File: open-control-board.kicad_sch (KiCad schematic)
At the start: 123 parts, among them CN1 Service boiler fill sensor, CN10 LCC Port, CN2 Water tank level switch, CN3 NTC Service Boiler, CN4 NTC Brew Boiler, CN5 Service boiler relay, CN6 Conn_02x04_Counter_Clockwise, CN7 Brew Switch, CN8 12V Separate Supply, CN9 Brew boiler relay, J1 USB_B_Micro, J10 Conn_01x04_Pin, J11 Conn_01x04_Pin, J12 Conn_02x06_Odd_Even, J13 Conn_02x05_Odd_Even, J14 Conn_02x04_Odd_Even, J15 Conn_02x05_Odd_Even, J16 USB_B_Micro, J18 Conn_01x03_Pin, J5 BM04B-SRSS-TB(LF)(SN), Q1 AO3401A, Q11 DMN63D8LDW, Q2 AO3401A, Q3 Q_PMOS-E_DUAL_Generic_SEP_S1G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, Q4 DMN63D8LDW, Q5 Q_PMOS-E_DUAL_Generic_SEP_S1G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, Q6 DMN63D8LDW, SW1 SW_Push, SW2 SW_Push, SW3 SW_Push, SW4 SW_Push, U10 FDC1004, U15 STPIC6C595TTR, U16 STPIC6C595TTR, U2 RP2040, U3 ESP32-S3-WROOM-1, U4 W25Q16JVUXIQ, U6 TPS82130, U7 TXB0108PWR, U8 ADS1115IDGS, Y1 XYDBPCNANF-12MHZ

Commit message: Clean up schematic and create PDF
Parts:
- removed unit 2 of Q4
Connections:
- no-connect marks 22 -> 19
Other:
- note added: "Power Management 5V @ 3A (Also powers 3V3) 3V3 @ 3A"
- note removed: "Power Management 5V @ 3A (Powers 3V3) 3V3 @ 3A"
- moved on the sheet: J5, JP4, JP5, JP6, Q3A, Q3B, Q4A, Q5B, Q6A, Q6B, R22, R23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

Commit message: R0B changes (WIP)
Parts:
- removed CN1: Service boiler fill sensor, Connector_PinHeader_2.54mm:PinHeader_1x02_P2.54mm_Vertical, symbol Connector:Conn_01x02_Pin
- removed J10, J11: Conn_01x04_Pin, Connector_PinSocket_2.54mm:PinSocket_1x04_P2.54mm_Vertical, symbol Connector:Conn_01x04_Pin
- removed J14: Conn_02x04_Odd_Even, Connector_PinHeader_2.54mm:PinHeader_2x04_P2.54mm_Vertical, symbol Connector_Generic:Conn_02x04_Odd_Even
- removed J18: Conn_01x03_Pin, Connector_PinHeader_2.54mm:PinHeader_1x03_P2.54mm_Vertical_SMD_Pin1Left, symbol Connector:Conn_01x03_Pin
- removed R31, R49, R50: 10K, Resistor_SMD:R_0402_1005Metric, symbol Device:R_Small
- removed U8: ADS1115IDGS, Package_SO:TSSOP-10_3x3mm_P0.5mm, symbol Analog_ADC:ADS1115IDGS
- added C26, C35, C36, C38, C39, C40, C41, C42: C_Small, Capacitor_SMD:C_0402_1005Metric_Pad0.74x0.62mm_HandSolder, symbol Device:C_Small
- added C43, C44: C_Small, Capacitor_SMD:C_0805_2012Metric_Pad1.18x1.45mm_HandSolder, symbol Device:C_Small
- added J3: Conn_02x03_Odd_Even, Connector_PinHeader_1.27mm:PinHeader_2x03_P1.27mm_Vertical_SMD, symbol Connector_Generic:Conn_02x03_Odd_Even
- added J4: Conn_01x06_Pin, Connector_PinHeader_2.54mm:PinHeader_1x06_P2.54mm_Vertical, symbol Connector:Conn_01x06_Pin
- added J5: Conn_02x05_Counter_Clockwise, Connector_PinHeader_2.54mm:PinHeader_2x05_P2.54mm_Vertical, symbol Connector_Generic:Conn_02x05_Odd_Even
- added J6: Conn_01x05_Pin, Connector_PinHeader_2.54mm:PinHeader_1x05_P2.54mm_Vertical, symbol Connector:Conn_01x05_Pin
- added JP1, JP10, JP11, JP12, JP16: SolderJumper_3_Bridged12, Jumper:SolderJumper-3_P1.3mm_Bridged2Bar12_RoundedPad1.0x1.5mm_NumberLabels, symbol Jumper:SolderJumper_3_Bridged12
- added JP14, JP15: SolderJumper_2_Open, Jumper:SolderJumper-2_P1.3mm_Open_RoundedPad1.0x1.5mm, symbol Jumper:SolderJumper_2_Open
- added JP17, JP18: SolderJumper_2_Bridged, Jumper:SolderJumper-2_P1.3mm_Bridged2Bar_RoundedPad1.0x1.5mm, symbol Jumper:SolderJumper_2_Bridged
- added unit 2 of Q4
- added unit 1 of Q5
- added Q7: DMN63D8LDW, PCM_Package_TO_SOT_SMD_AKL:SOT-363_SC-70-6, symbol PCM_Transistor_MOSFET_AKL:DMN63D8LDW
- added R14, R15, R40, R41, R42, R43: R_Small, Resistor_SMD:R_0805_2012Metric_Pad1.20x1.40mm_HandSolder, symbol Device:R_Small
- added R16, R25, R4: R_Small, Resistor_SMD:R_0402_1005Metric_Pad0.72x0.64mm_HandSolder, symbol Device:R_Small
- added R3: 10K, Resistor_SMD:R_0402_1005Metric, symbol Device:R_Small
- added RN3: 10K, PCM_Resistor_SMD_AKL:R_Array_Concave_4x0402, symbol PCM_Resistor_US_AKL:R_4x0402_Sep_Convex
- added U11, U12: ADS1115IDGS, Package_SO:TSSOP-10_3x3mm_P0.5mm, symbol Analog_ADC:ADS1115IDGS
- added U8: TXB0108PWR, Package_SO:TSSOP-20_4.4x6.5mm_P0.65mm, symbol Logic_LevelTranslator:TXS0108EPW
- CN10, CN3, CN4, CN6, CN8: Digikey (none) -> https://www.digikey.se/en/products/detail/te-connectivity-a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
- CN2: value Water tank level switch -> ~; Digikey (none) -> https://www.digikey.se/en/products/detail/te-connectivity-a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
- CN5: value Service boiler relay -> ~; Digikey (none) -> https://www.digikey.se/en/products/detail/te-connectivity-a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
- CN7: value Brew Switch -> ~; Digikey (none) -> https://www.digikey.se/en/products/detail/te-connectivity-a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
- CN9: value Brew boiler relay -> ~; Digikey (none) -> https://www.digikey.se/en/products/detail/te-connectivity-a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
- J1, J16: footprint U-D-M5DS-W-3:U-D-M5DS-W-3 -> Connector_USB:USB_Micro-B_Molex-105133-0001; LCSC C2909202 -> C782257
- JP3, JP7: footprint Connector_PinHeader_2.54mm:PinHeader_1x02_P2.54mm_Vertical -> Connector_PinHeader_1.27mm:PinHeader_1x02_P1.27mm_Vertical
- R19: value R_Small -> 10K; footprint Resistor_THT:R_Axial_DIN0204_L3.6mm_D1.6mm_P5.08mm_Horizontal -> Resistor_SMD:R_0402_1005Metric; Comment Hand solder -> (none); LCSC (none) -> C25744; now in the parts list
- R24, R26, R27: footprint Resistor_THT:R_Axial_DIN0204_L3.6mm_D1.6mm_P5.08mm_Horizontal -> Resistor_SMD:R_0402_1005Metric_Pad0.72x0.64mm_HandSolder; Comment Hand solder -> (none); now in the parts list
- U7: symbol Logic_LevelTranslator:TXB0108DQSR -> Logic_LevelTranslator:TXS0108EPW
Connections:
- net ADS1115_RDY_AVCC is gone; now on net INT_SCL_AVCC: Q4.6 (D1)
- net AIN1 is gone; now on net VOUT_4_GATE: R19.2
- net +12V: now also CN2.1 (Pin_1), CN5.1 (Pin_1), JP3.2 (B), JP7.2 (B), J3.2 (Pin_2), JP16.1 (A); no longer CN5.2 (Pin_2), CN9.1 (Pin_1)
- net +3V3: now also RN2.7 (R2.2), RN2.8 (R1.2), U7.2 (VCCA), Q4.5 (G2), RN3.5 (R4.2), RN3.6 (R3.2), U8.2 (VCCA); no longer J12.2 (Pin_2), RN2.5 (R4.2), RN2.6 (R3.2), U7.5 (VCCA)
- net +5V: now also J12.2 (Pin_2), U7.19 (VCCB), JP16.3 (B), U8.19 (VCCB); no longer JP3.2 (B), JP7.2 (B), U7.16 (VCCB)
- net AGND: now also C35.1, C36.1, C39.1, C40.2, C41.1, C42.2, J4.6 (Pin_6), JP17.1 (A), JP18.1 (A), U11.1 (ADDR), U11.3 (GND), U12.3 (GND); no longer R19.1, R24.1, R26.2, R27.1
- net AVCC: now also RN2.5 (R4.2), RN2.6 (R3.2), J4.1 (Pin_1), R14.1, R15.1, R40.1, R41.1, R42.1, R43.1, RN3.7 (R2.2), RN3.8 (R1.2), U11.8 (VDD), U12.1 (ADDR), U12.8 (VDD); no longer CN3.1 (Pin_1), CN4.1 (Pin_1), RN2.7 (R2.2), RN2.8 (R1.2)
- net BREW_SW: now also CN9.1 (Pin_1); no longer CN7.1 (Pin_1)
- net CIN1: now also J5.8 (Pin_8)
- net CIN2: now also J5.9 (Pin_9)
- net CIN3: now also J5.4 (Pin_4)
- net CIN4: now also J5.2 (Pin_2)
- net CN5_DRAIN: now also CN5.2 (Pin_2); no longer CN5.1 (Pin_1)
- net CN6_2_3V3: now also U7.4 (A3); no longer U7.1 (A1)
- net CN6_2_5V: now also U7.17 (B3); no longer U7.18 (B3)
- net CN6_3_3V3: now also U7.3 (A2); no longer U7.2 (A2)
- net CN6_3_5V: now also U7.18 (B2); no longer U7.19 (B2)
- net CN6_4_3V3: now also U7.1 (A1); no longer U7.3 (A3)
- net CN9_DRAIN: now also CN2.2 (Pin_2); no longer CN9.2 (Pin_2)
- net C_SHIELD_1: now also J5.10 (Pin_10), J5.7 (Pin_7)
- net C_SHIELD_2: now also J5.3 (Pin_3), J5.5 (Pin_5), J5.6 (Pin_6)
- net ESP32_EN: now also J3.1 (Pin_1)
- net ESP32_GPIO0: now also J3.6 (Pin_6)
- net ESP32_QWIIC_SCL: now also U3.19 (GPIO11/TOUCH11/ADC2_CH0/FSPID/FSPIIO5/SUBSPID); no longer U3.39 (GPIO1/TOUCH1/ADC1_CH0)
- net ESP32_QWIIC_SDA: now also U3.18 (GPIO10/TOUCH10/ADC1_CH9/FSPICS0/FSPIIO4/SUBSPICS0); no longer U3.38 (GPIO2/TOUCH2/ADC1_CH1)
- net ESP32_RP2040_UART1: now also U2.6 (GPIO4), U3.39 (GPIO1/TOUCH1/ADC1_CH0); no longer U2.13 (GPIO10), U3.11 (GPIO18/U1RXD/ADC2_CH7/CLK_OUT3)
- net ESP32_RP2040_UART2: now also U2.7 (GPIO5), U3.38 (GPIO2/TOUCH2/ADC1_CH1); no longer U2.14 (GPIO11), U3.23 (GPIO21)
- net GND: now also CN9.2 (Pin_2), U7.11 (GND), J3.4 (Pin_4), J5.1 (Pin_1), J6.1 (Pin_1), Q7.1 (S1), Q7.3 (D2), R3.2, U8.11 (GND); no longer CN2.2 (Pin_2), U7.15 (GND)
- net GP18: now also JP1.2 (C); no longer U2.29 (GPIO18), U3.4 (GPIO4/TOUCH4/ADC1_CH3)
- net GP19: now also JP10.2 (C); no longer U2.30 (GPIO19), U3.5 (GPIO5/TOUCH5/ADC1_CH4)
- net GP20: now also JP11.2 (C); no longer U2.31 (GPIO20), U3.6 (GPIO6/TOUCH6/ADC1_CH5)
- net GP21: now also JP12.2 (C); no longer U2.32 (GPIO21), U3.7 (GPIO7/TOUCH7/ADC1_CH6)
- net GP26: no longer U3.12 (GPIO8/TOUCH8/ADC1_CH7/SUBSPICS1)
- net GP27: no longer U3.17 (GPIO9/TOUCH9/ADC1_CH8/FSPIHD/SUBSPIHD)
- net GP28: no longer U3.18 (GPIO10/TOUCH10/ADC1_CH9/FSPICS0/FSPIIO4/SUBSPICS0)
- net GP29: no longer U3.19 (GPIO11/TOUCH11/ADC2_CH0/FSPID/FSPIIO5/SUBSPID)
- net INT_SCL: now also Q4.1 (S1), R20.1, RN2.1 (R1.1), U2.12 (GPIO9); no longer Q6.4 (S2), R21.1, RN2.4 (R4.1), U2.11 (GPIO8)
- net INT_SCL_AVCC: now also RN2.4 (R4.1), U11.10 (SCL), U12.10 (SCL); no longer Q6.3 (D2), RN2.2 (R2.1)
- net INT_SDA: now also R21.1, RN2.2 (R2.1), U2.11 (GPIO8), Q4.4 (S2); no longer Q6.1 (S1), R20.1, RN2.3 (R3.1), U2.12 (GPIO9)
- net INT_SDA_AVCC: now also RN2.3 (R3.1), Q4.3 (D2), U11.9 (SDA), U12.9 (SDA); no longer Q6.6 (D1), RN2.1 (R1.1)
- net QWIIC_SCL: now also U2.9 (GPIO7); no longer U2.8 (GPIO6)
- net QWIIC_SDA: now also U2.8 (GPIO6); no longer U2.9 (GPIO7)
- net RCLK_3V3: now also U7.6 (A5); no longer U7.7 (A5)
- net RCLK_5V: now also U7.15 (B5); no longer U7.14 (B5)
- net RP2040_BOOTSEL: now also Q7.6 (D1)
- net RP2040_RESETn: now also Q7.4 (S2)
- net SER_IN_3V3: now also U7.9 (A8); no longer U7.10 (A8)
- net SER_IN_5V: now also U7.12 (B8); no longer U7.11 (B8)
- net SRCK_3V3: now also U2.13 (GPIO10), U7.5 (A4); no longer U2.6 (GPIO4), U7.4 (A4)
- net SRCK_5V: now also U7.16 (B4); no longer U7.17 (B4)
- net SRCLR_3V3: now also U7.8 (A7); no longer U7.9 (A7)
- net SRCLR_5V: now also U7.13 (B7); no longer U7.12 (B7)
- net SR_OE: now also U7.10 (OE), R3.1, U8.10 (OE); no longer U7.6 (OE)
- net VOUT_1: now also J6.2 (Pin_2)
- net VOUT_2: now also J6.3 (Pin_3), Q5.6 (D1); no longer Q3.6 (D1)
- net VOUT_2_GATE: now also Q5.1 (G1); no longer Q3.1 (G1)
- net VOUT_3: now also J6.4 (Pin_4)
- net WATER_TANK_LVL_SW: now also CN7.1 (Pin_1); no longer CN2.1 (Pin_1)
- net nG_3V3: now also U7.7 (A6); no longer U7.8 (A6)
- net nG_5V: now also U7.14 (B6); no longer U7.13 (B6)
- net at JP5.2 (C), R29.1: now also Q5.5 (S1); no longer Q3.5 (S1)
- net at R12.1: now also U3.12 (GPIO8/TOUCH8/ADC1_CH7/SUBSPICS1); no longer U3.25 (GPIO48/SPICLK_N/SUBSPICLK_N_DIFF)
- net ESP32_U0RXD: now reaches U3.36 (U0RXD/GPIO44/CLK_OUT2)
- net ESP32_U0RXD: now also J3.3 (Pin_3)
- net ESP32_U0TXD: now reaches U3.37 (U0TXD/GPIO43/CLK_OUT1)
- net ESP32_U0TXD: now also J3.5 (Pin_5)
- net ESP32_BOOTSEL_RP2040: now reaches U3.8 (GPIO15/U0RTS/ADC2_CH4/XTAL_32K_P)
- net ESP32_BOOTSEL_RP2040: now also Q7.2 (G1)
- net ESP32_DISABLE_RP2040: now reaches U3.9 (GPIO16/U0CTS/ADC2_CH5/XTAL_32K_N)
- net ESP32_DISABLE_RP2040: now also Q7.5 (G2)
- net VOUT_4_GATE: now reaches U16.12 (DRAIN5)
- net VOUT_4_GATE: now also Q3.1 (G1)
- removed net ADS1115_RDY: Q4.1 (S1), U2.7 (GPIO5)
- net AIN0 renamed ADC2_AIN0
- net ADC2_AIN0: now also C39.2, C43.1, U12.4 (AIN0)
- net BREW_BOILER_NTC renamed ADC1_AIN1
- net ADC1_AIN1: now also C26.2, JP18.2 (B), U11.5 (AIN1); no longer R27.2
- net GP15 renamed RP2040_SERIAL_BOOT
- net SERVICE_BOILER_NTC renamed ADC1_AIN3
- net ADC1_AIN3: now also C38.2, JP17.2 (B), U11.7 (AIN3); no longer R26.1
- new net: JP16.2 (C), Q3.5 (S1), R19.1
- new net ADC1_AIN0: C26.1, C35.2, R4.2, U11.4 (AIN0)
- new net ADC1_AIN0_COND: CN4.1 (Pin_1), R14.2, R4.1
- new net ADC1_AIN2: C36.2, C38.1, R16.2, U11.6 (AIN2)
- new net ADC1_AIN2_COND: CN3.1 (Pin_1), R15.2, R16.1
- new net ADC2_AIN0_COND: J4.2 (Pin_2), R24.1, R40.2
- new net ADC2_AIN1: C40.1, C43.2, R25.2, U12.5 (AIN1)
- new net ADC2_AIN1_COND: J4.3 (Pin_3), R25.1, R41.2
- new net ADC2_AIN2: C41.2, C44.1, R26.2, U12.6 (AIN2)
- new net ADC2_AIN2_COND: J4.4 (Pin_4), R26.1, R42.2
- new net ADC2_AIN3: C42.1, C44.2, R27.2, U12.7 (AIN3)
- new net ADC2_AIN3_COND: J4.5 (Pin_5), R27.1, R43.2
- new net ADS1115_1_RDY: JP14.2 (B), Q6.1 (S1), RN3.4 (R4.1)
- new net ADS1115_1_RDY_AVCC: Q6.6 (D1), RN3.1 (R1.1), U11.2 (ALERT/RDY)
- new net ADS1115_2_RDY: JP15.2 (B), Q6.4 (S2), RN3.3 (R3.1)
- new net ADS1115_2_RDY_AVCC: Q6.3 (D2), RN3.2 (R2.1), U12.2 (ALERT/RDY)
- new net GP18_3V3: JP1.1 (A), JP14.1 (A), U2.29 (GPIO18), U3.4 (GPIO4/TOUCH4/ADC1_CH3), U8.5 (A4)
- new net GP18_5V: JP1.3 (B), U8.16 (B4)
- new net GP19_3V3: JP10.1 (A), JP15.1 (A), U2.30 (GPIO19), U3.5 (GPIO5/TOUCH5/ADC1_CH4), U8.4 (A3)
- new net GP19_5V: JP10.3 (B), U8.17 (B3)
- new net GP20_3V3: JP11.1 (A), U2.31 (GPIO20), U3.6 (GPIO6/TOUCH6/ADC1_CH5), U8.3 (A2)
- new net GP20_5V: JP11.3 (B), U8.18 (B2)
- new net GP21_3V3: JP12.1 (A), U2.32 (GPIO21), U3.7 (GPIO7/TOUCH7/ADC1_CH6), U8.1 (A1)
- new net GP21_5V: JP12.3 (B), U8.20 (B1)
- new net VOUT_4: J6.5 (Pin_5), Q3.6 (D1)
- no-connect marks 19 -> 28
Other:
- note added: "ADS1119 ADCs"
- note removed: "ADS1115 ADC"
- moved on the sheet: C28, C29, CN3, CN8, FB1, FB2, JP13, U7

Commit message: WIP
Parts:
- removed C35, C36: C_Small, Capacitor_SMD:C_0402_1005Metric_Pad0.74x0.62mm_HandSolder, symbol Device:C_Small
- C26, C38, C39, C40, C41, C42: value C_Small -> 100 nF; LCSC (none) -> C307331
- C43, C44: value C_Small -> 100 nF; LCSC (none) -> C77082; now not fitted
- R14, R15, R40, R41, R42, R43: now not fitted
- R16, R24, R25, R26, R27, R4: value R_Small -> 1K; LCSC (none) -> C11702
- U10: LCSC C2865994 -> C2652063
- U11, U12: LCSC (none) -> C37593

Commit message: Renamed connectors and added a lot of silk screen
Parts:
- U7, U8: value TXB0108PWR -> TXS0108EPWR; LCSC C53406 -> C17206
- renumbered CN10 to CN1, CN5 to CN10, CN2 to CN11, CN9 to CN12, CN7 to CN13, J12 to CN14, JP2 to CN2, CN8 to CN3, J5 to CN4, CN4 to CN5, CN3 to CN6, J4 to CN7, J6 to CN8, CN6 to CN9
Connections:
- net CN10_12V_GATE renamed CN1_12V_GATE
- net CN10_3V3_GATE renamed CN1_3V3_GATE
- net CN10_UART_RX renamed CN1_UART_RX
- net CN10_UART_RX_SHIFT_SEL renamed CN1_UART_RX_SHIFT_SEL
- net CN10_UART_TX renamed CN1_UART_TX
- net CN10_UART_TX_SHIFT_SEL renamed CN1_UART_TX_SHIFT_SEL
- net CN10_UART_VCC renamed CN1_UART_VCC
- net CN5_DRAIN renamed CN10_DRAIN
- net CN6_2_3V3 renamed CN9_2_3V3
- net CN6_2_5V renamed CN9_2_5V
- net CN6_3_3V3 renamed CN9_3_3V3
- net CN6_3_5V renamed CN9_3_5V
- net CN6_4 renamed CN9_4
- net CN6_4_3V3 renamed CN9_4_3V3
- net CN6_4_5V renamed CN9_4_5V
- net CN6_6 renamed CN9_6
- net CN6_8 renamed CN9_8
- net CN9_DRAIN renamed CN11_DRAIN
- net JP2_FA10 renamed CN2_FA10
- net JP2_FA7 renamed CN2_FA7
- net JP2_FA8 renamed CN2_FA8
- net JP2_FA9 renamed CN2_FA9
- no-connect marks 28 -> 29
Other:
- note added: "CN1 UART Level Shifter"
- note removed: "CN10 UART Level Shifter"

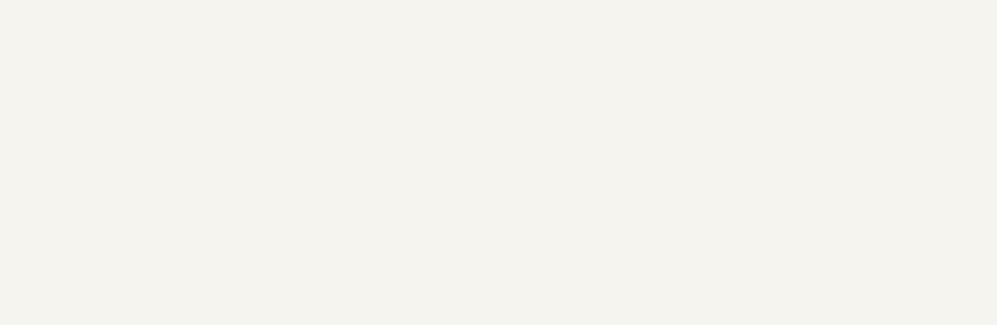
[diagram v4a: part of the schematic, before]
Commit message: Changed mounting holes to M2 (to match HV board) and use actual footprints
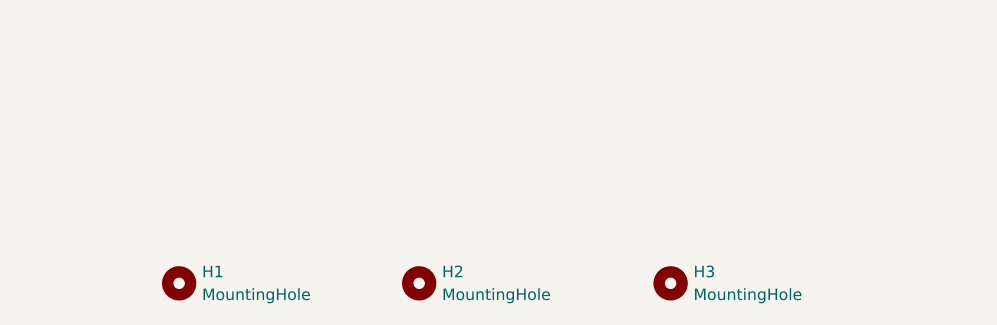
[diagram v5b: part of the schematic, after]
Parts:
- added H1, H2, H3: MountingHole, MountingHole_2.2mm_M2, symbol Mechanical:MountingHole
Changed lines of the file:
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@@
+    )
+  )
+  (symbol (lib_id "Mechanical:MountingHole") (at 99.06 728.98 0) (unit 1)
+    (in_bom yes) (on_board yes) (dnp no) (fields_autoplaced)
+    (property "Reference" "H2" (at 101.6 727.71 0)
+      (effects (font (size 1.27 1.27)) (justify left))
+    )
+    (property "Value" "MountingHole" (at 101.6 730.25 0)
+      (effects (font (size 1.27 1.27)) (justify left))
+    )
+    (property "Footprint" "MountingHole_2.2mm_M2" (at 99.06 728.98 0)
+      (effects (font (size 1.27 1.27)) hide)
+    )
+    (property "Datasheet" "~" (at 99.06 728.98 0)
+      (effects (font (size 1.27 1.27)) hide)
+    )
+    (instances
+      (project "open-control-board"
+        (path "/c7c8c763-88fa-419b-8f4a-ebade330cc39"
+          (reference "H2") (unit 1)
+        )
+      )
     )
   )
@@
     )
   )
+  (symbol (lib_id "Mechanical:MountingHole") (at 127 728.98 0) (unit 1)
+    (in_bom yes) (on_board yes) (dnp no) (fields_autoplaced)
+    (property "Reference" "H3" (at 129.54 727.71 0)
+      (effects (font (size 1.27 1.27)) (justify left))
+    )
+    (property "Value" "MountingHole" (at 129.54 730.25 0)
+      (effects (font (size 1.27 1.27)) (justify left))
+    )
+    (property "Footprint" "MountingHole_2.2mm_M2" (at 127 728.98 0)
+      (effects (font (size 1.27 1.27)) hide)
+    )
+    (property "Datasheet" "~" (at 127 728.98 0)
+      (effects (font (size 1.27 1.27)) hide)
+    )
+    (instances
+      (project "open-control-board"
+        (path "/c7c8c763-88fa-419b-8f4a-ebade330cc39"
+          (reference "H3") (unit 1)
+        )
+      )
+    )
+  )
   (symbol (lib_id "Device:R_Small") (at 577.85 181.61 90) (unit 1)
     (in_bom yes) (on_board yes) (dnp no)
@@
         )
       )
+    )
+  )
+  (symbol (lib_id "Mechanical:MountingHole") (at 72.39 728.98 0) (unit 1)
+    (in_bom yes) (on_board yes) (dnp no) (fields_autoplaced)
+    (property "Reference" "H1" (at 74.93 727.71 0)
+      (effects (font (size 1.27 1.27)) (justify left))
+    )
+    (property "Value" "MountingHole" (at 74.93 730.25 0)
+      (effects (font (size 1.27 1.27)) (justify left))
+    )
+    (property "Footprint" "MountingHole_2.2mm_M2" (at 72.39 728.98 0)
+      (effects (font (size 1.27 1.27)) hide)
+    )
+    (property "Datasheet" "~" (at 72.39 728.98 0)
+      (effects (font (size 1.27 1.27)) hide)
+    )
+    (instances
+      (project "open-control-board"
+        (path "/c7c8c763-88fa-419b-8f4a-ebade330cc39"
+          (reference "H1") (unit 1)
+        )
+      )

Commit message: Fixes
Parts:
- U10: LCSC C2652063 -> C2865994
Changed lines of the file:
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@@
       (effects (font (size 1.27 1.27)) hide)
     )
-    (property "LCSC" "C2652063" (at 308.61 388.62 0)
+    (property "LCSC" "C2865994" (at 308.61 388.62 0)
       (effects (font (size 1.27 1.27)) hide)
     )

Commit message: Added optional 5V level shifting for CN12-13
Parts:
- added JP19, JP2: SolderJumper_3_Bridged12, Jumper:SolderJumper-3_P1.3mm_Bridged2Bar12_RoundedPad1.0x1.5mm_NumberLabels, symbol Jumper:SolderJumper_3_Bridged12
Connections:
- net GP22_5V: now reaches U8.14 (B6)
- net GP22_5V: now also JP2.3 (B)
- net GP23_5V: now reaches U8.15 (B5)
- net GP23_5V: now also JP19.3 (B)
- net GP23_3V3: now reaches U8.6 (A5)
- net GP23_3V3: now also U2.35 (GPIO23), JP19.1 (A)
- net GP22_3V3: now reaches U8.7 (A6)
- net GP22_3V3: now also U2.34 (GPIO22), JP2.1 (A)
- net BREW_SW renamed GP22
- net GP22: now also JP2.2 (C); no longer U2.34 (GPIO22)
- net WATER_TANK_LVL_SW renamed GP23
- net GP23: now also JP19.2 (C); no longer U2.35 (GPIO23)
- no-connect marks 29 -> 25
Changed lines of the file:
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@@
   (junction (at 613.41 311.15) (diameter 0) (color 0 0 0 0)
   )
-  (no_connect (at 201.93 374.65))
   (no_connect (at 615.95 118.11))
   (no_connect (at 615.95 115.57))
@@
   (no_connect (at 615.95 120.65))
   (no_connect (at 524.51 115.57))
-  (no_connect (at 201.93 401.32))
   (no_connect (at 561.34 184.15))
   (no_connect (at 207.01 374.65))
-  (no_connect (at 204.47 401.32))
   (no_connect (at 615.95 105.41))
   (no_connect (at 43.18 226.06))
   (no_connect (at 209.55 374.65))
   (no_connect (at 615.95 87.63))
-  (no_connect (at 204.47 374.65))
   (no_connect (at 43.18 223.52))
   (no_connect (at 496.57 166.37))
@@
     )
   )
+  (global_label "GP22_3V3" (shape bidirectional) (at 280.67 566.42 0) (fields_autoplaced)
+    (effects (font (size 1.27 1.27)) (justify left))
+    (property "Intersheetrefs" "${INTERSHEET_REFS}" (at 294.2007 566.42 0)
+      (effects (font (size 1.27 1.27)) (justify left) hide)
+    )
+  )
+  (global_label "GP23" (shape bidirectional) (at 275.59 590.55 90) (fields_autoplaced)
+    (effects (font (size 1.27 1.27)) (justify left))
+    (property "Intersheetrefs" "${INTERSHEET_REFS}" (at 275.59 581.4945 90)
+      (effects (font (size 1.27 1.27)) (justify left) hide)
+    )
+  )
   (global_label "VOUT_4_GATE" (shape input) (at 613.41 320.04 270) (fields_autoplaced)
     (effects (font (size 1.27 1.27)) (justify right))
@@
     )
   )
+  (global_label "GP22_5V" (shape bidirectional) (at 204.47 374.65 90) (fields_autoplaced)
+    (effects (font (size 1.27 1.27)) (justify left))
+    (property "Intersheetrefs" "${INTERSHEET_REFS}" (at 204.47 362.3288 90)
+      (effects (font (size 1.27 1.27)) (justify left) hide)
+    )
+  )
   (global_label "GP20" (shape bidirectional) (at 82.55 107.95 0) (fields_autoplaced)
     (effects (font (size 1.27 1.27)) (justify left))
@@
     )
   )
-  (global_label "BREW_SW" (shape input) (at 353.06 170.18 0) (fields_autoplaced)
+  (global_label "GP22_3V3" (shape input) (at 353.06 170.18 0) (fields_autoplaced)
     (effects (font (size 1.27 1.27)) (justify left))
-    (property "Intersheetrefs" "${INTERSHEET_REFS}" (at 364.8141 170.18 0)
+    (property "Intersheetrefs" "${INTERSHEET_REFS}" (at 365.4794 170.18 0)
       (effects (font (size 1.27 1.27)) (justify left) hide)
     )
   )
+  (global_label "GP22_5V" (shape bidirectional) (at 270.51 566.42 180) (fields_autoplaced)
+    (effects (font (size 1.27 1.27)) (justify right))
+    (property "Intersheetrefs" "${INTERSHEET_REFS}" (at 258.1888 566.42 0)
+      (effects (font (size 1.27 1.27)) (justify right) hide)
+    )
+  )
   (global_label "ESP32_TDI" (shape bidirectional) (at 509.27 166.37 0) (fields_autoplaced)
     (effects (font (size 1.27 1.27)) (justify left))
@@
     )
   )
-  (global_label "WATER_TANK_LVL_SW" (shape input) (at 353.06 172.72 0) (fields_autoplaced)
+  (global_label "GP23_3V3" (shape input) (at 353.06 172.72 0) (fields_autoplaced)
     (effects (font (size 1.27 1.27)) (justify left))
-    (property "Intersheetrefs" "${INTERSHEET_REFS}" (at 375.337 172.72 0)
+    (property "Intersheetrefs" "${INTERSHEET_REFS}" (at 365.4794 172.72 0)
       (effects (font (size 1.27 1.27)) (justify left) hide)
     )
@@
     )
   )
+  (global_label "GP23_5V" (shape bidirectional) (at 270.51 594.36 180) (fields_autoplaced)
+    (effects (font (size 1.27 1.27)) (justify right))
+    (property "Intersheetrefs" "${INTERSHEET_REFS}" (at 258.1888 594.36 0)
+      (effects (font (size 1.27 1.27)) (justify right) hide)
+    )
+  )
   (global_label "GP27" (shape bidirectional) (at 353.06 185.42 0) (fields_autoplaced)
     (effects (font (size 1.27 1.27)) (justify left))
@@
     )
   )
+  (global_label "GP22_3V3" (shape bidirectional) (at 204.47 401.32 270) (fields_autoplaced)
+    (effects (font (size 1.27 1.27)) (justify right))
+    (property "Intersheetrefs" "${INTERSHEET_REFS}" (at 204.47 414.8507 90)
+      (effects (font (size 1.27 1.27)) (justify right) hide)
+    )
+  )
   (global_label "CN1_UART_TX_SHIFT_SEL" (shape input) (at 63.5 172.72 0) (fields_autoplaced)
     (effects (font (size 1.27 1.27)) (justify left))
@@
     )
   )
+  (global_label "GP23_3V3" (shape bidirectional) (at 280.67 594.36 0) (fields_autoplaced)
+    (effects (font (size 1.27 1.27)) (justify left))
+    (property "Intersheetrefs" "${INTERSHEET_REFS}" (at 294.2007 594.36 0)
+      (effects (font (size 1.27 1.27)) (justify left) hide)
+    )
+  )
   (global_label "GP21_5V" (shape bidirectional) (at 270.51 541.02 180) (fields_autoplaced)
     (effects (font (size 1.27 1.27)) (justify right))
@@
     )
   )
-  (global_label "BREW_SW" (shape output) (at 33.02 59.69 0) (fields_autoplaced)
+  (global_label "GP22" (shape output) (at 33.02 59.69 0) (fields_autoplaced)
     (effects (font (size 1.27 1.27)) (justify left))
-    (property "Intersheetrefs" "${INTERSHEET_REFS}" (at 44.7741 59.69 0)
+    (property "Intersheetrefs" "${INTERSHEET_REFS}" (at 40.9642 59.69 0)
       (effects (font (size 1.27 1.27)) (justify left) hide)
     )
@@
     )
   )
-  (global_label "WATER_TANK_LVL_SW" (shape output) (at 31.75 119.38 0) (fields_autoplaced)
+  (global_label "GP23" (shape output) (at 31.75 119.38 0) (fields_autoplaced)
     (effects (font (size 1.27 1.27)) (justify left))
-    (property "Intersheetrefs" "${INTERSHEET_REFS}" (at 54.027 119.38 0)
+    (property "Intersheetrefs" "${INTERSHEET_REFS}" (at 39.6942 119.38 0)
       (effects (font (size 1.27 1.27)) (justify left) hide)
     )
@@
     )
   )
+  (global_label "GP23_3V3" (shape bidirectional) (at 201.93 401.32 270) (fields_autoplaced)
+    (effects (font (size 1.27 1.27)) (justify right))
+    (property "Intersheetrefs" "${INTERSHEET_REFS}" (at 201.93 414.8507 90)
+      (effects (font (size 1.27 1.27)) (justify right) hide)
+    )
+  )
   (global_label "RP2040_QSPI_SD2" (shape bidirectional) (at 302.26 142.24 180) (fields_autoplaced)
     (effects (font (size 1.27 1.27)) (justify right))
@@
     )
   )
+  (global_label "GP22" (shape bidirectional) (at 275.59 562.61 90) (fields_autoplaced)
+    (effects (font (size 1.27 1.27)) (justify left))
+    (property "Intersheetrefs" "${INTERSHEET_REFS}" (at 275.59 553.5545 90)
+      (effects (font (size 1.27 1.27)) (justify left) hide)
+    )
+  )
   (global_label "RP2040_QSPI_CSn" (shape input) (at 375.92 57.15 180) (fields_autoplaced)
     (effects (font (size 1.27 1.27)) (justify right))
@@
     )
   )
+  (global_label "GP23_5V" (shape bidirectional) (at 201.93 374.65 90) (fields_autoplaced)
+    (effects (font (size 1.27 1.27)) (justify left))
+    (property "Intersheetrefs" "${INTERSHEET_REFS}" (at 201.93 362.3288 90)
+      (effects (font (size 1.27 1.27)) (justify left) hide)
+    )
+  )
   (global_label "ADC2_AIN3_COND" (shape passive) (at 123.19 612.14 180) (fields_autoplaced)
     (effects (font (size 1.27 1.27)) (justify right))
@@
     )
   )
+  (symbol (lib_id "Jumper:SolderJumper_3_Bridged12") (at 275.59 566.42 180) (unit 1)
+    (in_bom no) (on_board yes) (dnp no) (fields_autoplaced)
+    (property "Reference" "JP2" (at 275.59 570.23 0)
+      (effects (font (size 1.27 1.27)))
+    )
+    (property "Value" "SolderJumper_3_Bridged12" (at 275.59 572.77 0)
+      (effects (font (size 1.27 1.27)))
+    )
+    (property "Footprint" "Jumper:SolderJumper-3_P1.3mm_Bridged2Bar12_RoundedPad1.0x1.5mm_NumberLabels" (at 275.59 566.42 0)
+      (effects (font (size 1.27 1.27)) hide)
+    )
+    (property "Datasheet" "~" (at 275.59 566.42 0)
+      (effects (font (size 1.27 1.27)) hide)
+    )
+    (property "Digikey" "" (at 275.59 566.42 0)
+      (effects (font (size 1.27 1.27)) hide)
+    )
+    (pin "1")
+    (pin "2")
+    (pin "3")
+    (instances
+      (project "open-control-board"
+        (path "/c7c8c763-88fa-419b-8f4a-ebade330cc39"
+          (reference "JP2") (unit 1)
+        )
+      )
+    )
+  )
   (symbol (lib_id "Device:R_Small") (at 577.85 181.61 90) (unit 1)
     (in_bom yes) (on_board yes) (dnp no)
@@
         )
       )
+    )
+  )
+  (symbol (lib_id "Jumper:SolderJumper_3_Bridged12") (at 275.59 594.36 180) (unit 1)
+    (in_bom no) (on_board yes) (dnp no) (fields_autoplaced)
+    (property "Reference" "JP19" (at 275.59 598.17 0)
+      (effects (font (size 1.27 1.27)))
+    )
+    (property "Value" "SolderJumper_3_Bridged12" (at 275.59 600.71 0)
+      (effects (font (size 1.27 1.27)))
+    )
+    (property "Footprint" "Jumper:SolderJumper-3_P1.3mm_Bridged2Bar12_RoundedPad1.0x1.5mm_NumberLabels" (at 275.59 594.36 0)
+      (effects (font (size 1.27 1.27)) hide)
+    )
+    (property "Datasheet" "~" (at 275.59 594.36 0)
+      (effects (font (size 1.27 1.27)) hide)
+    )
+    (property "Digikey" "" (at 275.59 594.36 0)
+      (effects (font (size 1.27 1.27)) hide)
+    )
+    (pin "1")
+    (pin "2")
+    (pin "3")
+    (instances
+      (project "open-control-board"
+        (path "/c7c8c763-88fa-419b-8f4a-ebade330cc39"
+          (reference "JP19") (unit 1)
+        )
+      )
